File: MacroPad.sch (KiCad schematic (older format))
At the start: 56 parts, among them J1 AVR-ISP-6, SW1 Rotary_Encoder_Switch, SW10 *, SW11 9, SW12 6, SW13 3, SW14 ., SW15 -, SW16 +, SW17 Enter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

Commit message: cambiando rutas
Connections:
- net col0: now also SW15.2, SW16.2, SW17.2, U1.39 (PF4); no longer SW1.S1, SW2.2, SW3.2, SW4.2, SW5.2, U1.36 (PF7)
- net col1: now also SW10.2, SW11.2, SW12.2, SW13.2, SW14.2, U1.38 (PF5); no longer SW6.2, SW7.2, SW8.2, SW9.2, U1.37 (PF6)
- net col2: now also SW6.2, SW7.2, SW8.2, SW9.2, U1.37 (PF6); no longer SW10.2, SW11.2, SW12.2, SW13.2, SW14.2, U1.38 (PF5)
- net col3: now also SW1.S1, SW2.2, SW3.2, SW4.2, SW5.2, U1.36 (PF7); no longer SW15.2, SW16.2, SW17.2, U1.39 (PF4)
- net hwb: now also U1.33 (~HWB~/PE2); no longer U1.1 (PE6)
- net miso: now also U1.12 (PB7); no longer U1.25 (PD4)
- net mosi: now also U1.10 (PB2); no longer U1.27 (PD7)
- net sck: now also U1.11 (PB3); no longer U1.26 (PD6)
- net ROW4: now reaches U1.28 (PB4)
- net ROW4: now also D13.2 (K), D16.2 (K), D4.2 (K)
- net S2: no longer names the net of SW1.S2
- net S2: now also D14.1 (A); no longer D17.1 (A)
- net row0 renamed ROW0
- net ROW0: now also U1.32 (PC7); no longer U1.33 (~HWB~/PE2)
- net row1 renamed ROW1
- net ROW1: now also U1.31 (PC6); no longer U1.32 (PC7)
- net row2 renamed ROW2
- net ROW2: now also U1.30 (PB6); no longer U1.31 (PC6)
- net row3 renamed ROW3
- net ROW3: now also U1.29 (PB5); no longer U1.30 (PB6)
- removed net row4: D13.2 (K), D16.2 (K), D4.2 (K), U1.29 (PB5)
- net sw10: no longer names the net of D9.1 (A)
- net sw10: now also SW6.1; no longer SW10.1
- net sw11: no longer names the net of SW11.1
- net sw11: now also D1.1 (A); no longer D10.1 (A)
- net sw12: no longer names the net of D11.1 (A)
- net sw12: now also SW3.1; no longer SW12.1
- net sw13: no longer names the net of D12.1 (A)
- net sw13: now also SW4.1; no longer SW13.1
- net sw14: no longer names the net of D13.1 (A), SW14.1
- net sw15: no longer names the net of SW15.1
- net sw15: now also D17.1 (A); no longer D14.1 (A)
- net sw16: no longer names the net of D15.1 (A)
- net sw16: now also SW2.1; no longer SW16.1
- net sw17: no longer names the net of D16.1 (A), SW17.1
- removed net sw2: D1.1 (A), SW2.1
- net sw3: no longer names the net of D2.1 (A)
- net sw3: now also SW12.1; no longer SW3.1
- net sw4: no longer names the net of D3.1 (A)
- net sw4: now also SW13.1; no longer SW4.1
- net sw5: no longer names the net of D4.1 (A), SW5.1
- net sw6: no longer names the net of D5.1 (A)
- net sw6: now also SW10.1; no longer SW6.1
- net sw7: no longer names the net of SW7.1
- net sw7: now also D10.1 (A); no longer D6.1 (A)
- net sw8: no longer names the net of D7.1 (A), SW8.1
- net sw9: no longer names the net of D8.1 (A), SW9.1
- new net: D6.1 (A), SW16.1
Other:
- moved on the sheet: D1, D10, D11, D12, D13, D14, D15, D16, D17, D2, D3, D4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

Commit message: ultimas partes
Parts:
- added FB1: 60@100Mhz, Inductor_SMD:L_0805_2012Metric_Pad1.15x1.40mm_HandSolder, symbol Device:Ferrite_Bead
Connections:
- net GND: now also FB1.1; no longer USB1.13 (SHIELD)
- net ROW0: now also U1.28 (PB4); no longer U1.32 (PC7)
- net ROW1: now also U1.29 (PB5); no longer U1.31 (PC6)
- net ROW3: now also U1.31 (PC6); no longer U1.29 (PB5)
- net ROW4: now also U1.32 (PC7); no longer U1.28 (PB4)
- net scl: now also U1.22 (PD5); no longer U1.8 (PB0)
- net sda: now also U1.21 (PD3); no longer U1.9 (PB1)
- new net Earth: FB1.2, USB1.13 (SHIELD)
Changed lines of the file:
@@
 Connection ~ 1600 6500
-Wire Wire Line
-	1600 6500 1600 6600
 Wire Wire Line
 	1500 6400 1700 6400
@@
 Text GLabel 10300 5450 2    50   Input ~ 0
 col3
-Text GLabel 10300 3550 2    50   Input ~ 0
+Text GLabel 10300 2950 2    50   Input ~ 0
 ROW0
-Text GLabel 10300 3450 2    50   Input ~ 0
+Text GLabel 10300 3050 2    50   Input ~ 0
 ROW1
 Text GLabel 10300 3150 2    50   Input ~ 0
 ROW2
-Text GLabel 10300 3050 2    50   Input ~ 0
+Text GLabel 10300 3450 2    50   Input ~ 0
 ROW3
-Text GLabel 10300 2950 2    50   Input ~ 0
+Text GLabel 10300 3550 2    50   Input ~ 0
 ROW4
-Text GLabel 10300 2550 2    50   Input ~ 0
+Text GLabel 10300 4250 2    50   Input ~ 0
 scl
-Text GLabel 10300 2650 2    50   Input ~ 0
+Text GLabel 10300 4050 2    50   Input ~ 0
 sda
 Text GLabel 10300 4950 2    50   Input ~ 0
@@
 Wire Wire Line
 	4200 2450 4950 2450
+$Comp
+L Device:Ferrite_Bead FB1
+U 1 1 609AC08F
+P 1050 7200
+F 0 "FB1" V 776 7200 50  0000 C CNN
+F 1 "60@100Mhz" V 867 7200 50  0000 C CNN
+F 2 "Inductor_SMD:L_0805_2012Metric_Pad1.15x1.40mm_HandSolder" V 980 7200 50  0001 C CNN
+F 3 "~" H 1050 7200 50  0001 C CNN
+	1    1050 7200
+	0    1    1    0
+$EndComp
+$Comp
+L power:GND #PWR0120
+U 1 1 609B2E37
+P 1250 7200
+F 0 "#PWR0120" H 1250 6950 50  0001 C CNN
+F 1 "GND" H 1255 7027 50  0000 C CNN
+F 2 "" H 1250 7200 50  0001 C CNN
+F 3 "" H 1250 7200 50  0001 C CNN
+	1    1250 7200
+	1    0    0    -1
+$EndComp
+$Comp
+L power:Earth #PWR0121
+U 1 1 609B4E2B
+P 850 7200
+F 0 "#PWR0121" H 850 6950 50  0001 C CNN
+F 1 "Earth" H 850 7050 50  0001 C CNN
+F 2 "" H 850 7200 50  0001 C CNN
+F 3 "~" H 850 7200 50  0001 C CNN
+	1    850  7200
+	1    0    0    -1
+$EndComp
+$Comp
+L power:Earth #PWR0122
+U 1 1 609B6094
+P 1600 6600
+F 0 "#PWR0122" H 1600 6350 50  0001 C CNN
+F 1 "Earth" H 1600 6450 50  0001 C CNN
+F 2 "" H 1600 6600 50  0001 C CNN
+F 3 "~" H 1600 6600 50  0001 C CNN
+	1    1600 6600
+	1    0    0    -1
+$EndComp
+Wire Wire Line
+	1200 7200 1250 7200
+Wire Wire Line
+	900  7200 850  7200
+$Comp
+L power:PWR_FLAG #FLG0101
+U 1 1 609DC0B5
+P 1250 7200
+F 0 "#FLG0101" H 1250 7275 50  0001 C CNN
+F 1 "PWR_FLAG" V 1250 7328 50  0000 L CNN
+F 2 "" H 1250 7200 50  0001 C CNN
+F 3 "~" H 1250 7200 50  0001 C CNN
+	1    1250 7200
+	0    1    1    0
+$EndComp
+Connection ~ 1250 7200
+$Comp
+L power:PWR_FLAG #FLG0102
+U 1 1 609DCE83
+P 850 7200
+F 0 "#FLG0102" H 850 7275 50  0001 C CNN
+F 1 "PWR_FLAG" V 850 7327 50  0000 L CNN
+F 2 "" H 850 7200 50  0001 C CNN
+F 3 "~" H 850 7200 50  0001 C CNN
+	1    850  7200
+	0    -1   -1   0
+$EndComp
+Connection ~ 850  7200
 $EndSCHEMATC

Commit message: final final
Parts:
- SW10, SW11, SW12, SW13, SW14, SW15, SW2, SW3, SW4, SW6, SW7, SW8, SW9: footprint kailh MX:Kailh_socket_MX -> kailh_switches:SW_Hotswap_Kailh_1.00u
- SW16, SW17: footprint kailh MX:Kailh_socket_MX -> kailh_switches:SW_Hotswap_Kailh_2.00u_Rotated
- SW5: footprint kailh MX:Kailh_socket_MX -> kailh_switches:SW_Hotswap_Kailh_2.00u
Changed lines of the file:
@@
 F 0 "SW11" H 4400 2435 50  0000 C CNN
 F 1 "9" H 4400 2344 50  0000 C CNN
-F 2 "kailh MX:Kailh_socket_MX" H 4400 2350 50  0001 C CNN
+F 2 "kailh_switches:SW_Hotswap_Kailh_1.00u" H 4400 2350 50  0001 C CNN
 F 3 "~" H 4400 2350 50  0001 C CNN
 	1    4400 2150
@@
 F 0 "SW8" H 3650 3135 50  0000 C CNN
 F 1 "5" H 3650 3044 50  0000 C CNN
-F 2 "kailh MX:Kailh_socket_MX" H 3650 3050 50  0001 C CNN
+F 2 "kailh_switches:SW_Hotswap_Kailh_1.00u" H 3650 3050 50  0001 C CNN
 F 3 "~" H 3650 3050 50  0001 C CNN
 	1    3650 2850
@@
 F 0 "SW12" H 4400 3135 50  0000 C CNN
 F 1 "6" H 4400 3044 50  0000 C CNN
-F 2 "kailh MX:Kailh_socket_MX" H 4400 3050 50  0001 C CNN
+F 2 "kailh_switches:SW_Hotswap_Kailh_1.00u" H 4400 3050 50  0001 C CNN
 F 3 "~" H 4400 3050 50  0001 C CNN
 	1    4400 2850
@@
 F 0 "SW4" H 2900 3835 50  0000 C CNN
 F 1 "1" H 2900 3744 50  0000 C CNN
-F 2 "kailh MX:Kailh_socket_MX" H 2900 3750 50  0001 C CNN
+F 2 "kailh_switches:SW_Hotswap_Kailh_1.00u" H 2900 3750 50  0001 C CNN
 F 3 "~" H 2900 3750 50  0001 C CNN
 	1    2900 3550
@@
 F 0 "SW9" H 3650 3835 50  0000 C CNN
 F 1 "2" H 3650 3744 50  0000 C CNN
-F 2 "kailh MX:Kailh_socket_MX" H 3650 3750 50  0001 C CNN
+F 2 "kailh_switches:SW_Hotswap_Kailh_1.00u" H 3650 3750 50  0001 C CNN
 F 3 "~" H 3650 3750 50  0001 C CNN
 	1    3650 3550
@@
 F 0 "SW13" H 4400 3835 50  0000 C CNN
 F 1 "3" H 4400 3744 50  0000 C CNN
-F 2 "kailh MX:Kailh_socket_MX" H 4400 3750 50  0001 C CNN
+F 2 "kailh_switches:SW_Hotswap_Kailh_1.00u" H 4400 3750 50  0001 C CNN
 F 3 "~" H 4400 3750 50  0001 C CNN
 	1    4400 3550
@@
 F 0 "SW14" H 4400 4535 50  0000 C CNN
 F 1 "." H 4400 4444 50  0000 C CNN
-F 2 "kailh MX:Kailh_socket_MX" H 4400 4450 50  0001 C CNN
+F 2 "kailh_switches:SW_Hotswap_Kailh_1.00u" H 4400 4450 50  0001 C CNN
 F 3 "~" H 4400 4450 50  0001 C CNN
 	1    4400 4250
@@
 F 0 "SW16" H 5150 2435 50  0000 C CNN
 F 1 "+" H 5150 2344 50  0000 C CNN
-F 2 "kailh MX:Kailh_socket_MX" H 5150 2350 50  0001 C CNN
+F 2 "kailh_switches:SW_Hotswap_Kailh_2.00u_Rotated" H 5150 2350 50  0001 C CNN
 F 3 "~" H 5150 2350 50  0001 C CNN
 	1    5150 2150
@@
 F 0 "SW17" H 5150 3835 50  0000 C CNN
 F 1 "Enter" H 5150 3744 50  0000 C CNN
-F 2 "kailh MX:Kailh_socket_MX" H 5150 3750 50  0001 C CNN
+F 2 "kailh_switches:SW_Hotswap_Kailh_2.00u_Rotated" H 5150 3750 50  0001 C CNN
 F 3 "~" H 5150 3750 50  0001 C CNN
 	1    5150 3550
@@
 F 0 "SW7" H 3650 2435 50  0000 C CNN
 F 1 "8" H 3650 2344 50  0000 C CNN
-F 2 "kailh MX:Kailh_socket_MX" H 3650 2350 50  0001 C CNN
+F 2 "kailh_switches:SW_Hotswap_Kailh_1.00u" H 3650 2350 50  0001 C CNN
 F 3 "~" H 3650 2350 50  0001 C CNN
 	1    3650 2150
@@
 F 0 "SW10" H 4400 1735 50  0000 C CNN
 F 1 "*" H 4400 1644 50  0000 C CNN
-F 2 "kailh MX:Kailh_socket_MX" H 4400 1650 50  0001 C CNN
+F 2 "kailh_switches:SW_Hotswap_Kailh_1.00u" H 4400 1650 50  0001 C CNN
 F 3 "~" H 4400 1650 50  0001 C CNN
 	1    4400 1450
@@
 F 0 "SW6" H 3650 1735 50  0000 C CNN
 F 1 "/" H 3650 1644 50  0000 C CNN
-F 2 "kailh MX:Kailh_socket_MX" H 3650 1650 50  0001 C CNN
+F 2 "kailh_switches:SW_Hotswap_Kailh_1.00u" H 3650 1650 50  0001 C CNN
 F 3 "~" H 3650 1650 50  0001 C CNN
 	1    3650 1450
@@
 F 0 "SW2" H 2900 2435 50  0000 C CNN
 F 1 "7" H 2900 2344 50  0000 C CNN
-F 2 "kailh MX:Kailh_socket_MX" H 2900 2350 50  0001 C CNN
+F 2 "kailh_switches:SW_Hotswap_Kailh_1.00u" H 2900 2350 50  0001 C CNN
 F 3 "~" H 2900 2350 50  0001 C CNN
 	1    2900 2150
@@
 F 0 "SW5" H 2900 4535 50  0000 C CNN
 F 1 "0" H 2900 4444 50  0000 C CNN
-F 2 "kailh MX:Kailh_socket_MX" H 2900 4450 50  0001 C CNN
+F 2 "kailh_switches:SW_Hotswap_Kailh_2.00u" H 2900 4450 50  0001 C CNN
 F 3 "~" H 2900 4450 50  0001 C CNN
 	1    2900 4250
@@
 F 0 "SW15" H 5150 1735 50  0000 C CNN
 F 1 "-" H 5150 1644 50  0000 C CNN
-F 2 "kailh MX:Kailh_socket_MX" H 5150 1650 50  0001 C CNN
+F 2 "kailh_switches:SW_Hotswap_Kailh_1.00u" H 5150 1650 50  0001 C CNN
 F 3 "~" H 5150 1650 50  0001 C CNN
 	1    5150 1450
@@
 F 0 "SW3" H 2900 3135 50  0000 C CNN
 F 1 "4" H 2900 3044 50  0000 C CNN
-F 2 "kailh MX:Kailh_socket_MX" H 2900 3050 50  0001 C CNN
+F 2 "kailh_switches:SW_Hotswap_Kailh_1.00u" H 2900 3050 50  0001 C CNN
 F 3 "~" H 2900 3050 50  0001 C CNN
 	1    2900 2850

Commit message: cambio de footprint
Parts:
- SW10, SW11, SW12, SW13, SW14, SW15, SW2, SW3, SW4, SW6, SW7, SW8, SW9: footprint kailh_switches:SW_Hotswap_Kailh_1.00u -> kailh MX:Kailh_socket_MX
- SW16, SW17: footprint kailh_switches:SW_Hotswap_Kailh_2.00u_Rotated -> kailh MX:Kailh_socket_MX
- SW5: footprint kailh_switches:SW_Hotswap_Kailh_2.00u -> kailh MX:Kailh_socket_MX
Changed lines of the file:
@@
 F 0 "SW11" H 4400 2435 50  0000 C CNN
 F 1 "9" H 4400 2344 50  0000 C CNN
-F 2 "kailh_switches:SW_Hotswap_Kailh_1.00u" H 4400 2350 50  0001 C CNN
+F 2 "kailh MX:Kailh_socket_MX" H 4400 2350 50  0001 C CNN
 F 3 "~" H 4400 2350 50  0001 C CNN
 	1    4400 2150
@@
 F 0 "SW8" H 3650 3135 50  0000 C CNN
 F 1 "5" H 3650 3044 50  0000 C CNN
-F 2 "kailh_switches:SW_Hotswap_Kailh_1.00u" H 3650 3050 50  0001 C CNN
+F 2 "kailh MX:Kailh_socket_MX" H 3650 3050 50  0001 C CNN
 F 3 "~" H 3650 3050 50  0001 C CNN
 	1    3650 2850
@@
 F 0 "SW12" H 4400 3135 50  0000 C CNN
 F 1 "6" H 4400 3044 50  0000 C CNN
-F 2 "kailh_switches:SW_Hotswap_Kailh_1.00u" H 4400 3050 50  0001 C CNN
+F 2 "kailh MX:Kailh_socket_MX" H 4400 3050 50  0001 C CNN
 F 3 "~" H 4400 3050 50  0001 C CNN
 	1    4400 2850
@@
 F 0 "SW4" H 2900 3835 50  0000 C CNN
 F 1 "1" H 2900 3744 50  0000 C CNN
-F 2 "kailh_switches:SW_Hotswap_Kailh_1.00u" H 2900 3750 50  0001 C CNN
+F 2 "kailh MX:Kailh_socket_MX" H 2900 3750 50  0001 C CNN
 F 3 "~" H 2900 3750 50  0001 C CNN
 	1    2900 3550
@@
 F 0 "SW9" H 3650 3835 50  0000 C CNN
 F 1 "2" H 3650 3744 50  0000 C CNN
-F 2 "kailh_switches:SW_Hotswap_Kailh_1.00u" H 3650 3750 50  0001 C CNN
+F 2 "kailh MX:Kailh_socket_MX" H 3650 3750 50  0001 C CNN
 F 3 "~" H 3650 3750 50  0001 C CNN
 	1    3650 3550
@@
 F 0 "SW13" H 4400 3835 50  0000 C CNN
 F 1 "3" H 4400 3744 50  0000 C CNN
-F 2 "kailh_switches:SW_Hotswap_Kailh_1.00u" H 4400 3750 50  0001 C CNN
+F 2 "kailh MX:Kailh_socket_MX" H 4400 3750 50  0001 C CNN
 F 3 "~" H 4400 3750 50  0001 C CNN
 	1    4400 3550
@@
 F 0 "SW14" H 4400 4535 50  0000 C CNN
 F 1 "." H 4400 4444 50  0000 C CNN
-F 2 "kailh_switches:SW_Hotswap_Kailh_1.00u" H 4400 4450 50  0001 C CNN
+F 2 "kailh MX:Kailh_socket_MX" H 4400 4450 50  0001 C CNN
 F 3 "~" H 4400 4450 50  0001 C CNN
 	1    4400 4250
@@
 F 0 "SW16" H 5150 2435 50  0000 C CNN
 F 1 "+" H 5150 2344 50  0000 C CNN
-F 2 "kailh_switches:SW_Hotswap_Kailh_2.00u_Rotated" H 5150 2350 50  0001 C CNN
+F 2 "kailh MX:Kailh_socket_MX" H 5150 2350 50  0001 C CNN
 F 3 "~" H 5150 2350 50  0001 C CNN
 	1    5150 2150
@@
 F 0 "SW17" H 5150 3835 50  0000 C CNN
 F 1 "Enter" H 5150 3744 50  0000 C CNN
-F 2 "kailh_switches:SW_Hotswap_Kailh_2.00u_Rotated" H 5150 3750 50  0001 C CNN
+F 2 "kailh MX:Kailh_socket_MX" H 5150 3750 50  0001 C CNN
 F 3 "~" H 5150 3750 50  0001 C CNN
 	1    5150 3550
@@
 F 0 "SW7" H 3650 2435 50  0000 C CNN
 F 1 "8" H 3650 2344 50  0000 C CNN
-F 2 "kailh_switches:SW_Hotswap_Kailh_1.00u" H 3650 2350 50  0001 C CNN
+F 2 "kailh MX:Kailh_socket_MX" H 3650 2350 50  0001 C CNN
 F 3 "~" H 3650 2350 50  0001 C CNN
 	1    3650 2150
@@
 F 0 "SW10" H 4400 1735 50  0000 C CNN
 F 1 "*" H 4400 1644 50  0000 C CNN
-F 2 "kailh_switches:SW_Hotswap_Kailh_1.00u" H 4400 1650 50  0001 C CNN
+F 2 "kailh MX:Kailh_socket_MX" H 4400 1650 50  0001 C CNN
 F 3 "~" H 4400 1650 50  0001 C CNN
 	1    4400 1450
@@
 F 0 "SW6" H 3650 1735 50  0000 C CNN
 F 1 "/" H 3650 1644 50  0000 C CNN
-F 2 "kailh_switches:SW_Hotswap_Kailh_1.00u" H 3650 1650 50  0001 C CNN
+F 2 "kailh MX:Kailh_socket_MX" H 3650 1650 50  0001 C CNN
 F 3 "~" H 3650 1650 50  0001 C CNN
 	1    3650 1450
@@
 F 0 "SW2" H 2900 2435 50  0000 C CNN
 F 1 "7" H 2900 2344 50  0000 C CNN
-F 2 "kailh_switches:SW_Hotswap_Kailh_1.00u" H 2900 2350 50  0001 C CNN
+F 2 "kailh MX:Kailh_socket_MX" H 2900 2350 50  0001 C CNN
 F 3 "~" H 2900 2350 50  0001 C CNN
 	1    2900 2150
@@
 Text GLabel 2700 3850 0    50   Input ~ 0
 ROW3
-Text GLabel 2800 1750 0    50   Input ~ 0
-ROW0
 Text GLabel 4250 6000 2    50   Input ~ 0
 D-
@@
 F 0 "SW5" H 2900 4535 50  0000 C CNN
 F 1 "0" H 2900 4444 50  0000 C CNN
-F 2 "kailh_switches:SW_Hotswap_Kailh_2.00u" H 2900 4450 50  0001 C CNN
+F 2 "kailh MX:Kailh_socket_MX" H 2900 4450 50  0001 C CNN
 F 3 "~" H 2900 4450 50  0001 C CNN
 	1    2900 4250
@@
 F 0 "SW15" H 5150 1735 50  0000 C CNN
 F 1 "-" H 5150 1644 50  0000 C CNN
-F 2 "kailh_switches:SW_Hotswap_Kailh_1.00u" H 5150 1650 50  0001 C CNN
+F 2 "kailh MX:Kailh_socket_MX" H 5150 1650 50  0001 C CNN
 F 3 "~" H 5150 1650 50  0001 C CNN
 	1    5150 1450
@@
 Text GLabel 4600 1450 1    50   Input ~ 0
 col1
-Text GLabel 3850 1450 1    50   Input ~ 0
-col2
-Text GLabel 3100 1250 1    50   Input ~ 0
-col3
 $Comp
 L Switch:SW_Push SW3
@@
 F 0 "SW3" H 2900 3135 50  0000 C CNN
 F 1 "4" H 2900 3044 50  0000 C CNN
-F 2 "kailh_switches:SW_Hotswap_Kailh_1.00u" H 2900 3050 50  0001 C CNN
+F 2 "kailh MX:Kailh_socket_MX" H 2900 3050 50  0001 C CNN
 F 3 "~" H 2900 3050 50  0001 C CNN
 	1    2900 2850
@@
 $EndComp
 Connection ~ 850  7200
+Text GLabel 3850 1450 1    50   Input ~ 0
+col2
+Text GLabel 3100 1250 1    50   Input ~ 0
+col3
+Text GLabel 2800 1750 0    50   Input ~ 0
+ROW0
 $EndSCHEMATC

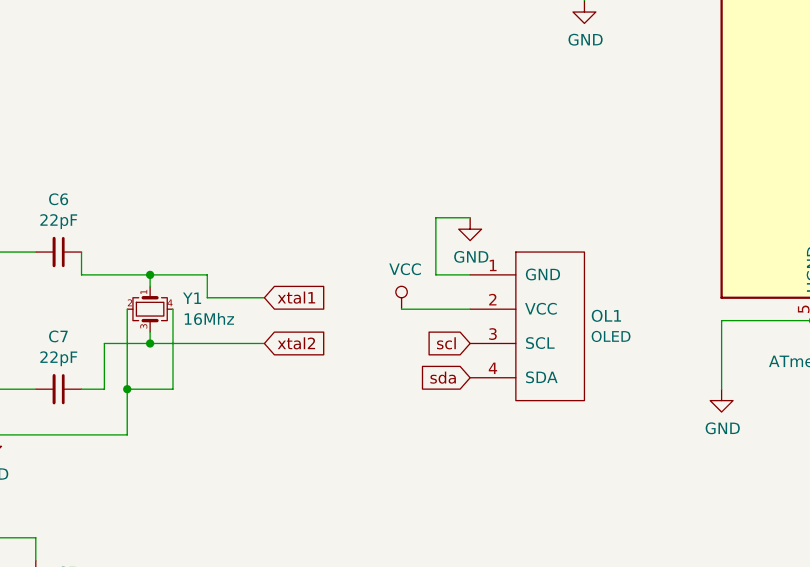
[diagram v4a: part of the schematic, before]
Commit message: cambiado tamaño pistas y vcc oled
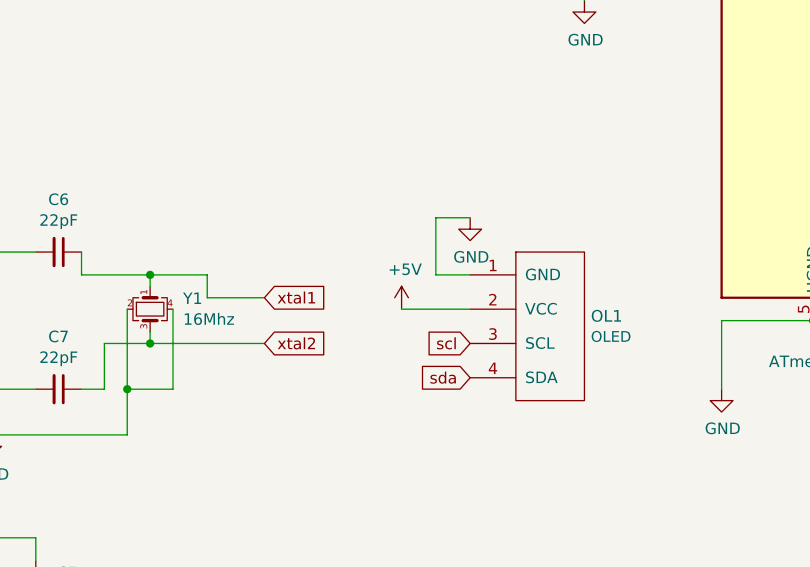
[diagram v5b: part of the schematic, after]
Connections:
- net +5V: now also OL1.2 (VCC)
- net VCC: no longer OL1.2 (VCC)
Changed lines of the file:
@@
 Wire Wire Line
 	7950 5400 8100 5400
-$Comp
-L power:VCC #PWR0119
-U 1 1 60C6BC64
-P 7800 5800
-F 0 "#PWR0119" H 7800 5650 50  0001 C CNN
-F 1 "VCC" H 7817 5973 50  0000 C CNN
-F 2 "" H 7800 5800 50  0001 C CNN
-F 3 "" H 7800 5800 50  0001 C CNN
-	1    7800 5800
-	1    0    0    -1
-$EndComp
 Wire Wire Line
 	8100 5800 7800 5800
@@
 Text GLabel 2800 1750 0    50   Input ~ 0
 ROW0
+$Comp
+L power:+5V #PWR?
+U 1 1 6099D0BA
+P 7800 5800
+F 0 "#PWR?" H 7800 5650 50  0001 C CNN
+F 1 "+5V" H 7815 5973 50  0000 C CNN
+F 2 "" H 7800 5800 50  0001 C CNN
+F 3 "" H 7800 5800 50  0001 C CNN
+	1    7800 5800
+	1    0    0    -1
+$EndComp
 $EndSCHEMATC
